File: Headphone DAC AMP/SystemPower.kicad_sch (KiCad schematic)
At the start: 37 parts, among them U1 NCV8187AMTW090TAG, U11 ADP5071AREZ-R7, U6 MCP1727-1802xSN, U7 MCP1727-3302xSN

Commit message: Routing Complete!
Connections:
- net Vin is gone; now on net 5Vin: C46.1, C47.1, U6.1 (Vin), U6.2 (Vin), U6.3 (~{SHDN}), U7.1 (Vin), U7.2 (Vin), U7.3 (~{SHDN})
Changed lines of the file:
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@@
 	)
 	(hierarchical_label "+6V"
-		(shape input)
+		(shape output)
 		(at 242.57 55.88 180)
-		(effects
-			(font
-				(size 1.27 1.27)
-			)
-			(justify right)
-		)
-	)
-	(hierarchical_label "GND"
-		(shape input)
-		(at 41.91 251.46 180)
-		(effects
-			(font
-				(size 1.27 1.27)
-			)
-			(justify right)
-		)
-	)
-	(hierarchical_label "Vin"
-		(shape input)
-		(at 35.56 165.1 180)
 		(effects
 			(font
@@
 		)
 	)
+	(hierarchical_label "GND"
+		(shape input)
+		(at 41.91 251.46 180)
+		(effects
+			(font
+				(size 1.27 1.27)
+			)
+			(justify right)
+		)
+	)
+	(hierarchical_label "5Vin"
+		(shape input)
+		(at 35.56 165.1 180)
+		(effects
+			(font
+				(size 1.27 1.27)
+			)
+			(justify right)
+		)
+	)
 	(hierarchical_label "0.9v"
+		(shape output)
+		(at 113.03 220.98 0)
+		(effects
+			(font
+				(size 1.27 1.27)
+			)
+			(justify left)
+		)
+	)
+	(hierarchical_label "5Vin"
 		(shape input)
-		(at 113.03 220.98 0)
+		(at 351.79 63.5 0)
 		(effects
 			(font
@@
 		)
 	)
-	(hierarchical_label "Vin"
+	(hierarchical_label "5Vin"
 		(shape input)
 		(at 34.29 100.33 180)
@@
 		)
 	)
-	(hierarchical_label "5Vin"
-		(shape input)
-		(at 351.79 63.5 0)
-		(effects
-			(font
-				(size 1.27 1.27)
-			)
-			(justify left)
-		)
-	)
 	(hierarchical_label "1.8v"
-		(shape input)
+		(shape output)
 		(at 113.03 165.1 0)
 		(effects
@@
 	)
 	(hierarchical_label "-6V"
-		(shape input)
+		(shape output)
 		(at 375.92 55.88 0)
 		(effects
@@
 	)
 	(hierarchical_label "3.3v"
-		(shape input)
+		(shape output)
 		(at 107.95 100.33 0)
 		(effects

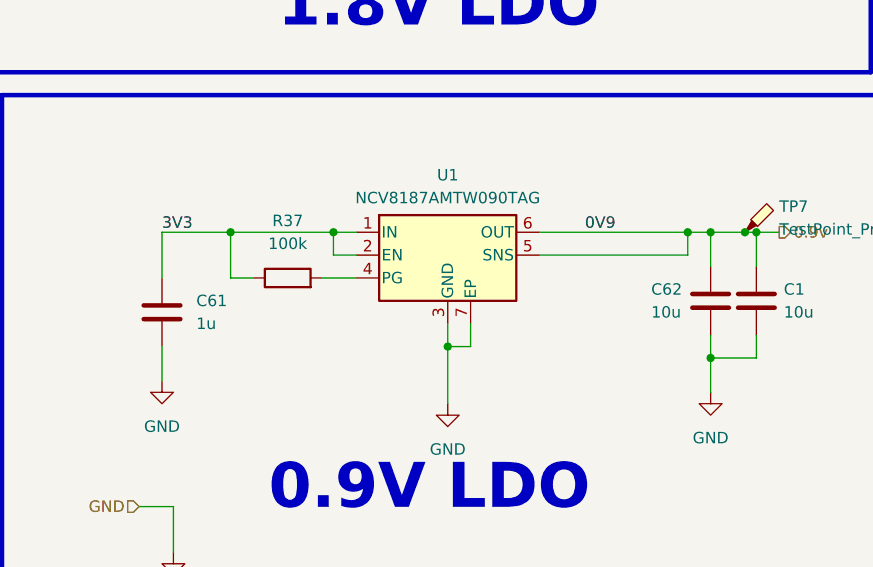
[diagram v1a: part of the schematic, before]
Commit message: Changed 0v9 regulator to TLV75709 SOP-23-5
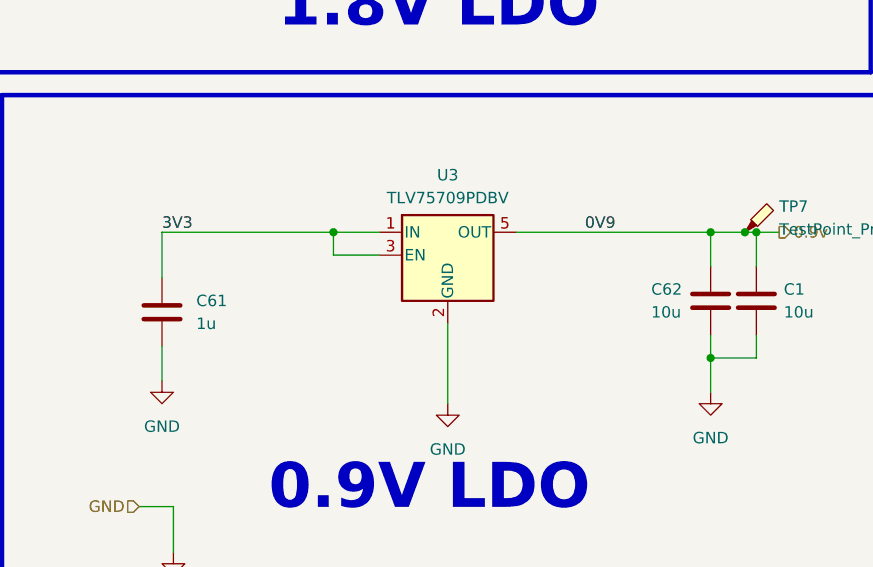
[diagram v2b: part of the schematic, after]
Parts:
- removed R37: 100k, Resistor_SMD:R_0805_2012Metric_Pad1.20x1.40mm_HandSolder, symbol Device:R
- removed U1: NCV8187AMTW090TAG, NCV8187AMTW090TAG:SON65P200X200X80-7N, symbol Regulator_Linear:LP38691SD-5.0
- added U3: TLV75709PDBV, Package_TO_SOT_SMD:SOT-23-5, symbol Regulator_Linear:TLV75709PDBV
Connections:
- net 0.9v: now also U3.5 (OUT)
- net 3.3v: now also U3.1 (IN), U3.3 (EN)
- net GND: now also U3.2 (GND)
